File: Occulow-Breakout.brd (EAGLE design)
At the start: 50.8 x 50.8 mm, 18 parts

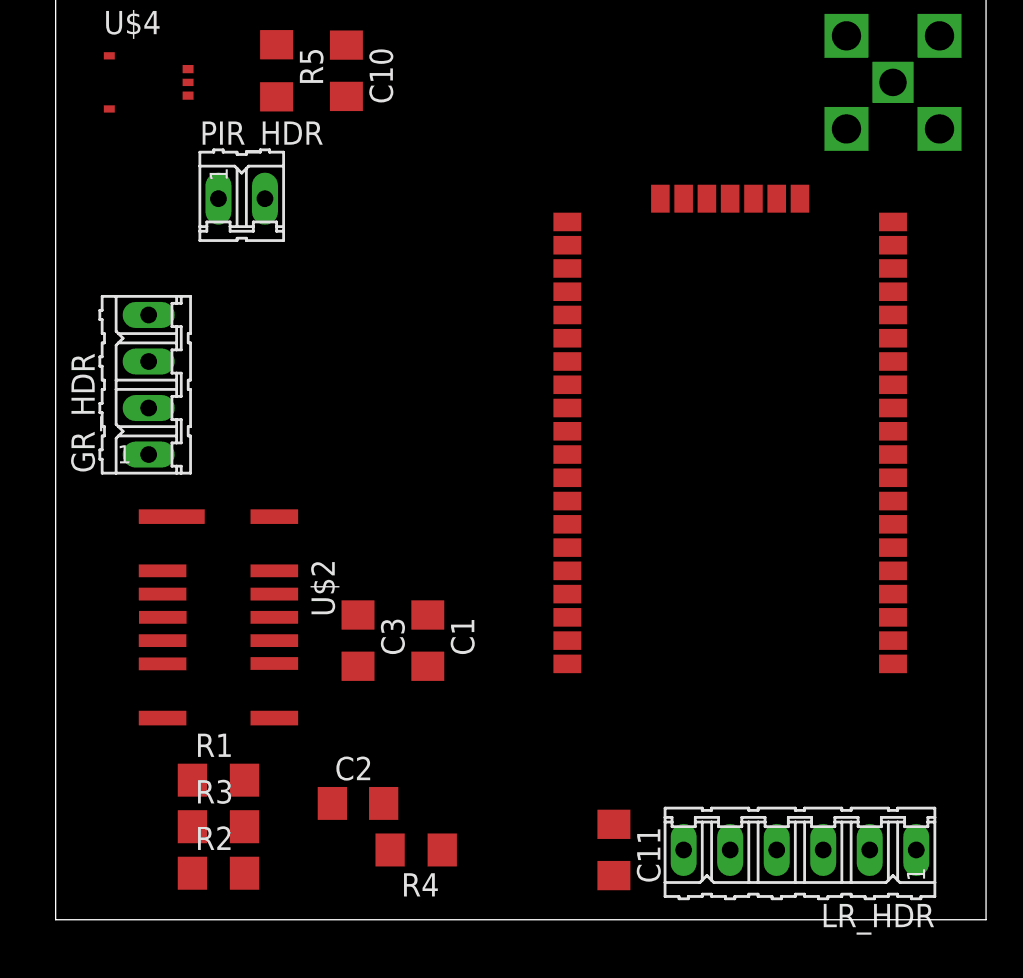
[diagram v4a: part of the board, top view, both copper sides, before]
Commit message: Ground pins on headers
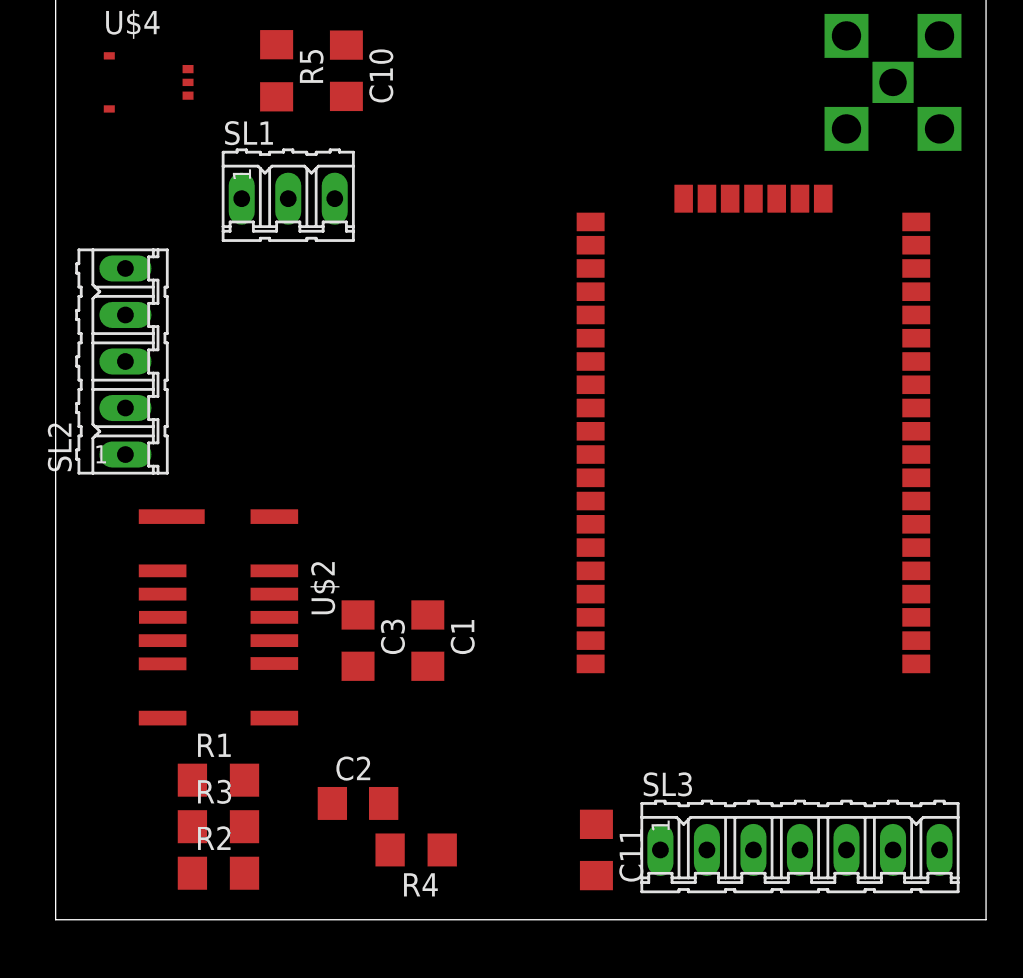
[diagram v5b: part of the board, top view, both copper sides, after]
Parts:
- removed GR_HDR: (no value), con-amp-quick:04P
- removed LR_HDR: (no value), con-amp-quick:06P
- removed PIR_HDR: (no value), con-amp-quick:02P
- added SL1: (no value), con-amp-quick:03P
- added SL2: (no value), con-amp-quick:05P
- added SL3: (no value), con-amp-quick:07P
- moved U$1 1.27 mm to (38.1, 25.4)
- moved C11 0.95 mm to (29.5, 3.81)
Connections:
- removed net N$11: LR_HDR.1
- net GND: now also SL1.2, SL2.4, SL3.6
- net GR_INT: now also SL2.1; no longer GR_HDR.1
- net GR_SCL: now also SL2.2; no longer GR_HDR.2
- net GR_SDA: now also SL2.3; no longer GR_HDR.3
- net GR_VCC: now also SL2.5; no longer GR_HDR.4
- net LR_CTS: now also SL3.2; no longer LR_HDR.2
- net LR_RST_N: now also SL3.5; no longer LR_HDR.5
- net LR_RTS: now also SL3.1
- net LR_RX: now also SL3.4; no longer LR_HDR.4
- net LR_TX: now also SL3.3; no longer LR_HDR.3
- net LR_VCC: now also SL3.7; no longer LR_HDR.6
- net PIR_OUT: now also SL1.1; no longer PIR_HDR.1
- net PIR_VCC: now also SL1.3; no longer PIR_HDR.2

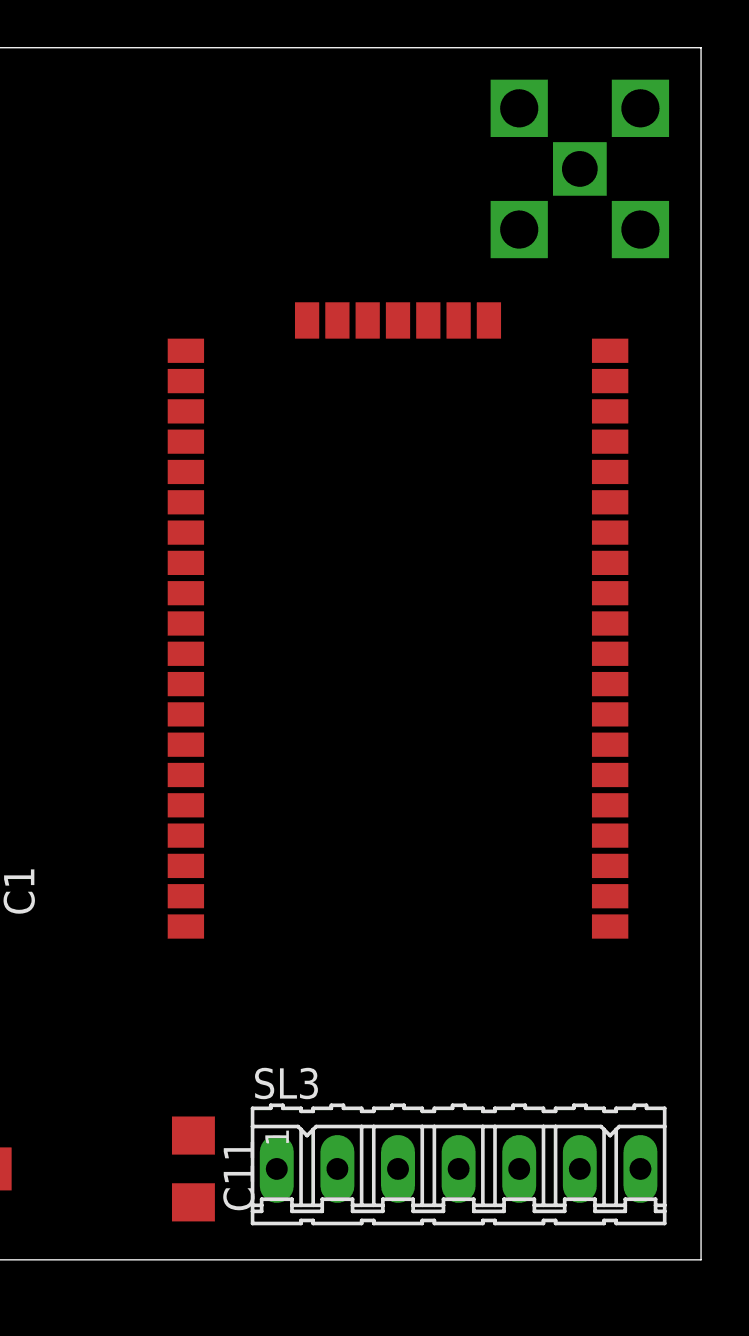
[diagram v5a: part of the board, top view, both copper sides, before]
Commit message: Routing for lora chip
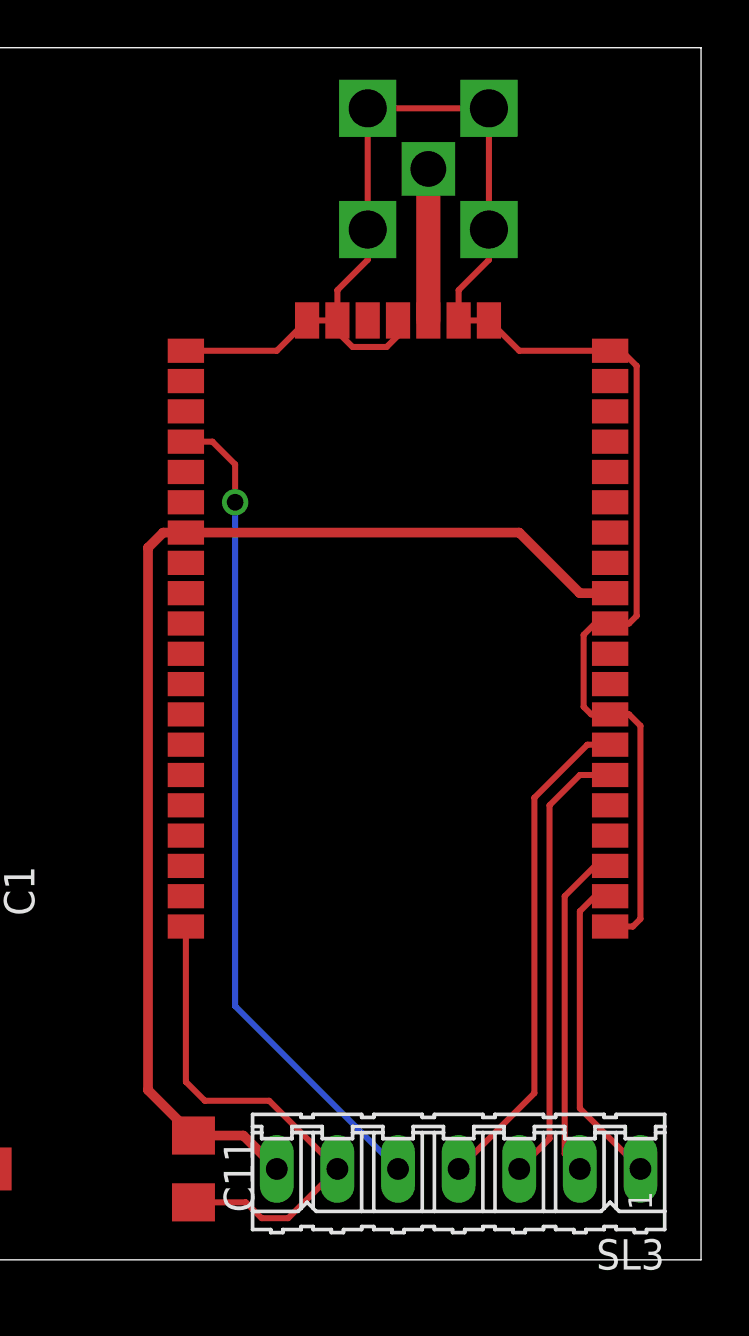
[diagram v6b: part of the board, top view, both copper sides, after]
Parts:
- moved U$3 6.35 mm to (39.4, 45.7)
- turned SL3 to 180 degrees
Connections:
- net N$1 renamed RF
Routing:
- net GND: track 0.00 -> 92.9 mm
- net LR_VCC: track 0.00 -> 50.2 mm
- net LR_RST_N: track 0.00 -> 34.8 mm, vias 0 -> 1
- net LR_RX: track 0.00 -> 21.0 mm
- net LR_TX: track 0.00 -> 18.8 mm
- net LR_CTS: track 0.00 -> 14.1 mm
- net LR_RTS: track 0.00 -> 13.4 mm
- net RF: track 0.00 -> 6.35 mm

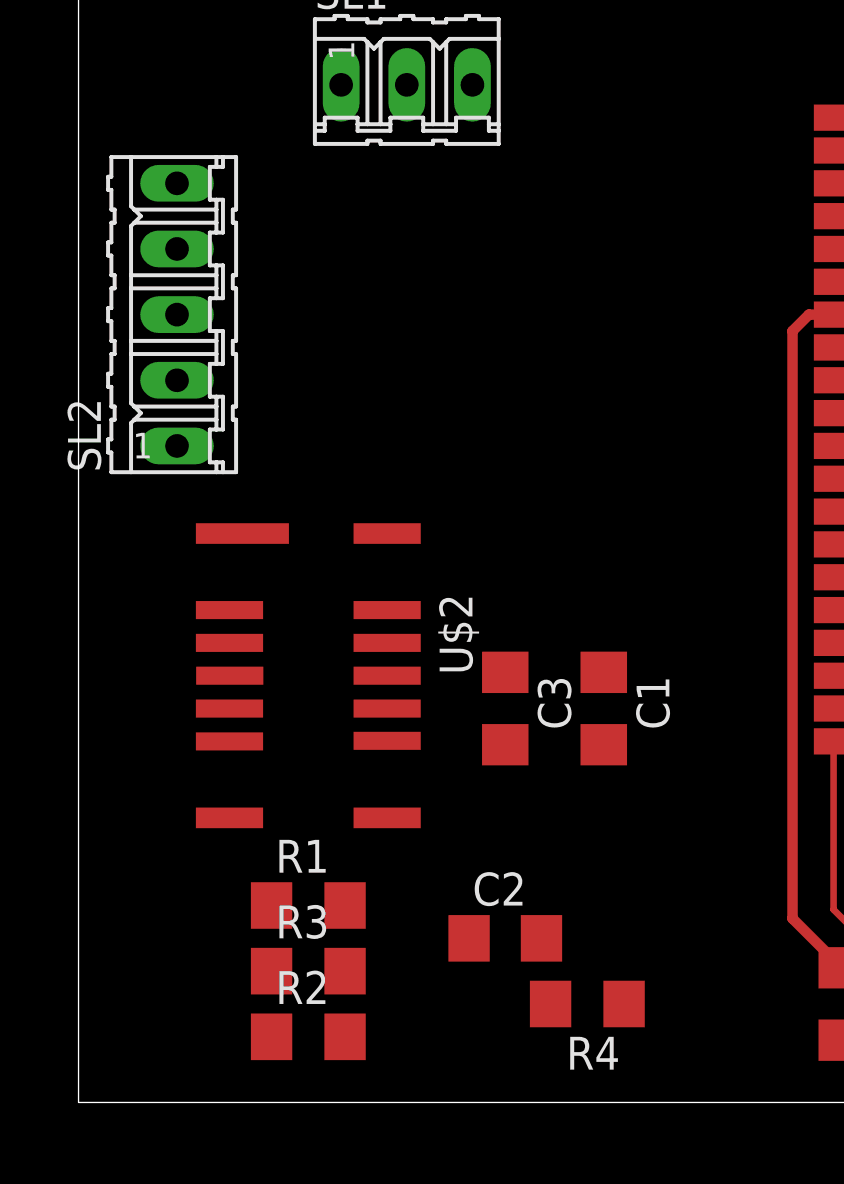
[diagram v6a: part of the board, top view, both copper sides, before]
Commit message: Routing for grideye
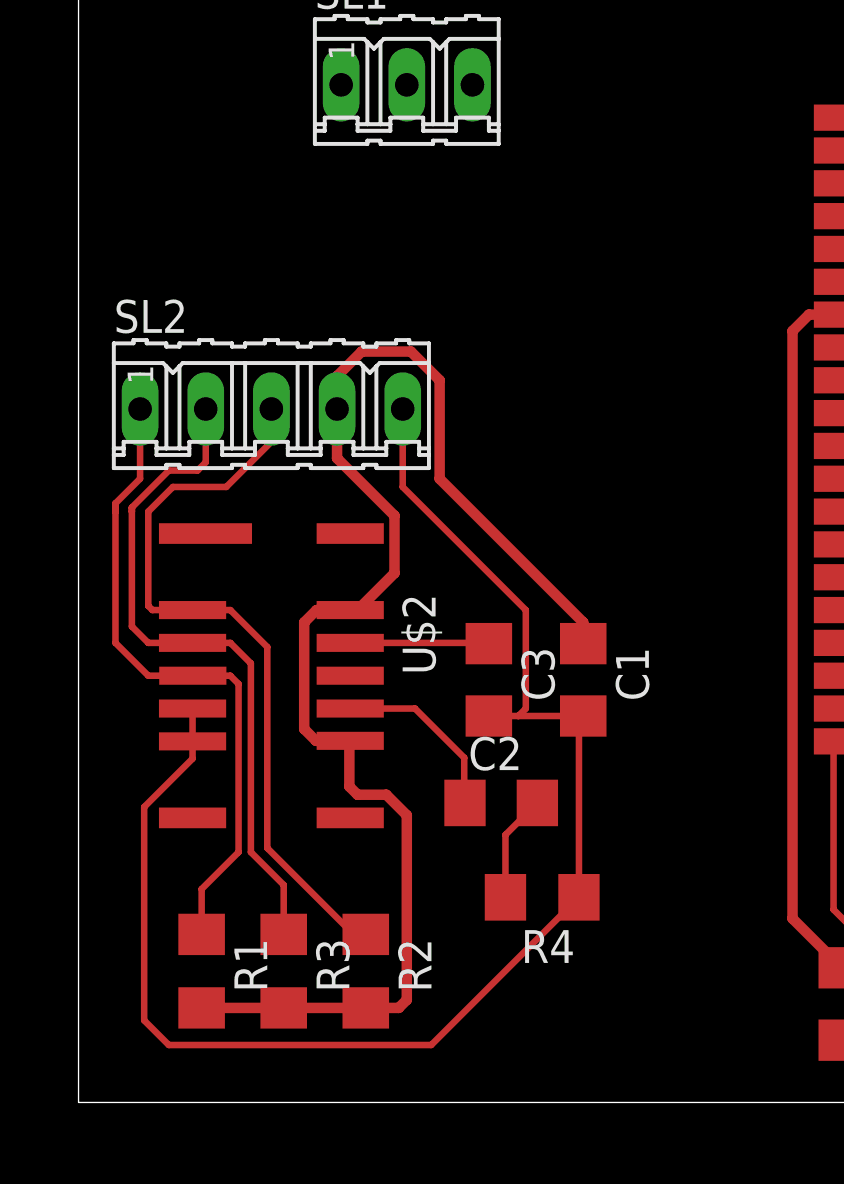
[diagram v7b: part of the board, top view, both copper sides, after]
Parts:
- moved C2 5.24 mm to (16.4, 11.6)
- moved SL2 5.16 mm to (7.46, 26.8), turned to 0 degrees
- moved R1 4.85 mm to (4.76, 5.08), turned to 270 degrees
- moved R4 4.48 mm to (17.9, 7.94)
- moved R2 3.38 mm to (11.1, 5.08), turned to 270 degrees
- moved U$2 1.43 mm to (7.46, 16.5)
- moved C1 1.37 mm to (19.5, 16.4)
- moved C3 1.28 mm to (15.9, 16.4)
- moved R3 0.95 mm to (7.94, 5.08), turned to 270 degrees
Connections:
- net GND: now also SL2.5; no longer SL2.4
- net GR_VCC: now also SL2.4; no longer SL2.5
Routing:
- net GND: track 92.9 -> 150.1 mm
- net GR_VCC: track 0.00 -> 56.0 mm
- net GR_SDA: track 0.00 -> 29.0 mm
- net GR_SCL: track 0.00 -> 26.6 mm
- net GR_INT: track 0.00 -> 25.5 mm
- net N$2: track 0.00 -> 6.96 mm
- net N$4: track 0.00 -> 5.38 mm
- net N$3: track 0.00 -> 4.16 mm

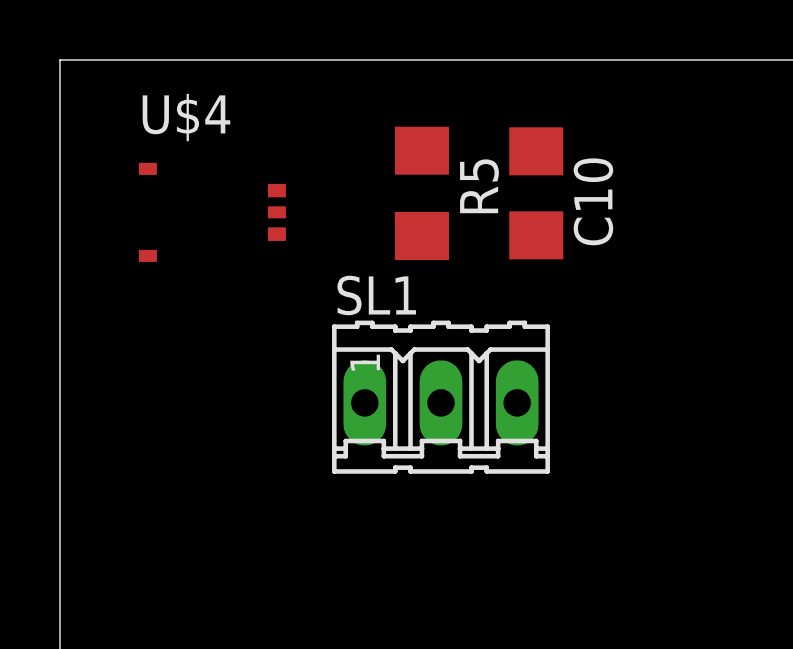
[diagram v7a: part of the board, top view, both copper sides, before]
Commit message: IR sensor layout
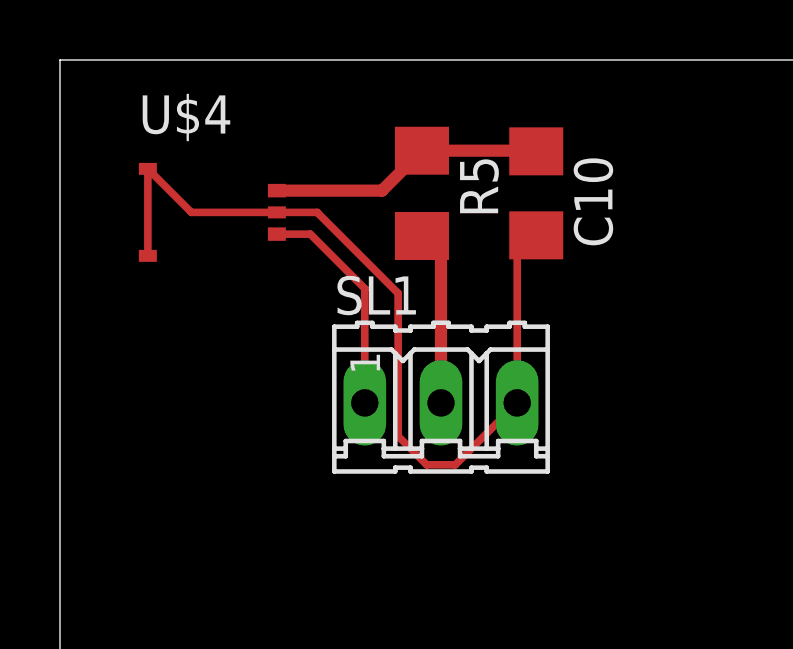
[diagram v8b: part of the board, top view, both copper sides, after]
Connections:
- net GND: now also SL1.3; no longer SL1.2
- net PIR_VCC: now also SL1.2; no longer SL1.3
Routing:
- net GND: track 150.1 -> 178.9 mm
- net N$5: track 0.00 -> 9.24 mm
- net PIR_OUT: track 0.00 -> 7.49 mm
- net PIR_VCC: track 0.00 -> 5.83 mm
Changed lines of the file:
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@@
 <contactref element="C10" pad="2"/>
 <contactref element="C11" pad="2"/>
-<contactref element="SL1" pad="2"/>
 <contactref element="SL3" pad="6"/>
 <wire x1="35.56" y1="39.37" x2="34.29" y2="39.37" width="0.254" layer="1"/>
@@
 <wire x1="12.54125" y1="23.8125" x2="12.54125" y2="26.82875" width="0.254" layer="1"/>
 <wire x1="19.52625" y1="14.95125" x2="17.015" y2="14.95125" width="0.254" layer="1"/>
+<contactref element="SL1" pad="3"/>
+<wire x1="2.93" y1="47.17" x2="2.93" y2="44.27" width="0.254" layer="1"/>
+<wire x1="4.38" y1="45.72" x2="7.23" y2="45.72" width="0.254" layer="1"/>
+<wire x1="4.38" y1="45.72" x2="2.93" y2="47.17" width="0.254" layer="1"/>
+<wire x1="7.23" y1="45.72" x2="8.5725" y2="45.72" width="0.254" layer="1"/>
+<wire x1="8.5725" y1="45.72" x2="11.27125" y2="43.02125" width="0.254" layer="1"/>
+<wire x1="11.27125" y1="43.02125" x2="11.27125" y2="38.25875" width="0.254" layer="1"/>
+<wire x1="11.27125" y1="38.25875" x2="12.22375" y2="37.30625" width="0.254" layer="1"/>
+<wire x1="12.22375" y1="37.30625" x2="13.17625" y2="37.30625" width="0.254" layer="1"/>
+<wire x1="13.17625" y1="37.30625" x2="15.24" y2="39.37" width="0.254" layer="1"/>
+<wire x1="15.24" y1="39.37" x2="15.24" y2="44.32" width="0.254" layer="1"/>
+<wire x1="15.24" y1="44.32" x2="15.875" y2="44.955" width="0.254" layer="1"/>
 <wire x1="29.21" y1="38.1" x2="29.21" y2="31.75" width="0" layer="19" extent="1-1"/>
 <wire x1="29.21" y1="21.59" x2="29.21" y2="31.75" width="0" layer="19" extent="1-1"/>
 <wire x1="29.21" y1="13.97" x2="29.21" y2="21.59" width="0" layer="19" extent="1-1"/>
 <wire x1="19.52625" y1="14.95125" x2="29.21" y2="13.97" width="0" layer="19" extent="1-1"/>
-<wire x1="12.7" y1="39.37" x2="12.54125" y2="26.82875" width="0" layer="19" extent="1-1"/>
-<wire x1="15.875" y1="44.955" x2="12.7" y2="39.37" width="0" layer="19" extent="1-1"/>
-<wire x1="7.23" y1="45.72" x2="12.7" y2="39.37" width="0" layer="19" extent="1-1"/>
-<wire x1="2.93" y1="47.17" x2="7.23" y2="45.72" width="0" layer="19" extent="1-1"/>
-<wire x1="2.93" y1="44.27" x2="2.93" y2="47.17" width="0" layer="19" extent="1-1"/>
+<wire x1="12.22375" y1="37.30625" x2="12.54125" y2="26.82875" width="0" layer="19" extent="1-1"/>
 </signal>
 <signal name="N$2">
@@
 <contactref element="C10" pad="1"/>
 <contactref element="R5" pad="1"/>
-<wire x1="12.065" y1="47.777" x2="15.875" y2="47.755" width="0" layer="19" extent="1-1"/>
-<wire x1="7.23" y1="46.445" x2="12.065" y2="47.777" width="0" layer="19" extent="1-1"/>
+<wire x1="15.875" y1="47.755" x2="15.853" y2="47.777" width="0.254" layer="1"/>
+<wire x1="7.23" y1="46.445" x2="10.733" y2="46.445" width="0.4064" layer="1"/>
+<wire x1="10.733" y1="46.445" x2="12.065" y2="47.777" width="0.4064" layer="1"/>
+<wire x1="12.065" y1="47.777" x2="15.853" y2="47.777" width="0.4064" layer="1"/>
+<wire x1="15.853" y1="47.777" x2="15.875" y2="47.755" width="0.4064" layer="1"/>
 </signal>
 <signal name="PIR_OUT">
 <contactref element="U$4" pad="1"/>
 <contactref element="SL1" pad="1"/>
-<wire x1="10.16" y1="39.37" x2="7.23" y2="44.995" width="0" layer="19" extent="1-1"/>
+<wire x1="7.23" y1="44.995" x2="8.345" y2="44.995" width="0.254" layer="1"/>
+<wire x1="8.345" y1="44.995" x2="10.16" y2="43.18" width="0.254" layer="1"/>
+<wire x1="10.16" y1="43.18" x2="10.16" y2="39.37" width="0.254" layer="1"/>
 </signal>
 <signal name="GR_VCC">
@@
 <signal name="PIR_VCC">
 <contactref element="R5" pad="2"/>
-<contactref element="SL1" pad="3"/>
-<wire x1="15.24" y1="39.37" x2="12.065" y2="44.933" width="0" layer="19" extent="1-1"/>
+<contactref element="SL1" pad="2"/>
+<wire x1="12.7" y1="39.37" x2="12.7" y2="44.298" width="0.4064" layer="1"/>
+<wire x1="12.7" y1="44.298" x2="12.065" y2="44.933" width="0.4064" layer="1"/>
 </signal>
 <signal name="LR_VCC">
